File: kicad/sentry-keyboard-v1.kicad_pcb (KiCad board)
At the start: 2 copper layers, 315 x 121 mm, 269 parts, among them J2 Conn_01x04, J4 AVR-ISP-6, SW1 Reset, SW2 RotaryEncoder_Switch, U1 ATmega32U4-AU, Y1 16Mhz

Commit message: Get all components roughly placed
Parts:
- moved D109 109.0 mm to (247.7, 156.2)
- moved D110 97.3 mm to (228.5, 156.4)
- moved D133 96.3 mm to (355.8, 158.2)
- moved D108 88.7 mm to (266.7, 156.2)
- moved D118 83.5 mm to (68.8, 156.2)
- moved D123 80.8 mm to (147.6, 137.2)
- moved D125 76.2 mm to (185.6, 137.1)
- moved D124 76.2 mm to (166.6, 137.2)
- moved D132 76.2 mm to (316.7, 156.2)
- moved D112 76.1 mm to (190.6, 156.2)
- moved D113 76.1 mm to (171.5, 156.2)
- moved D114 76.1 mm to (152.4, 156.2)
- moved D115 76.1 mm to (133.5, 156.2)
- moved D116 76.1 mm to (114.5, 156.2)
- moved D127 76.0 mm to (223.6, 137.0)
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
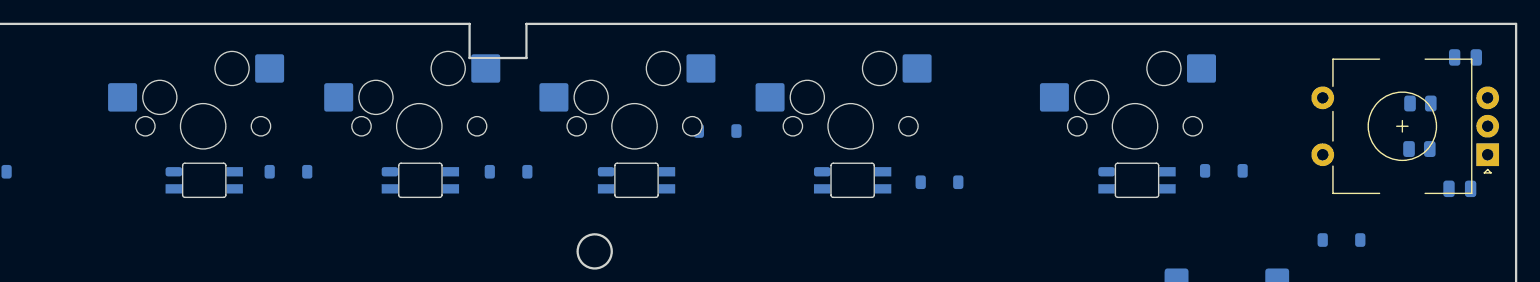
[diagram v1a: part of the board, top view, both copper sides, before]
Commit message: Get the last footprints roughed in.
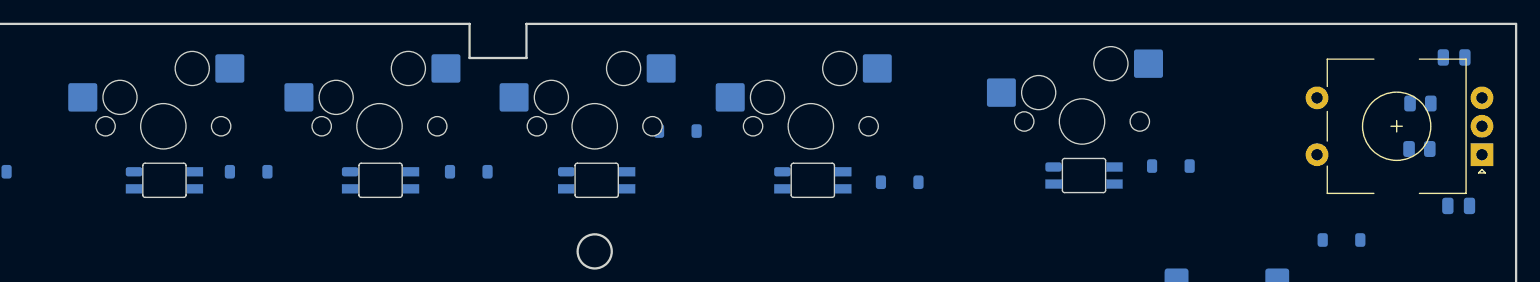
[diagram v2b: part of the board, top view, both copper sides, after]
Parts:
- moved D164 4.68 mm to (328.5, 94.8)
- moved D35 4.68 mm to (336.1, 94.0)
- moved F13 4.68 mm to (328.3, 90.1)
- moved D160 3.50 mm to (247.7, 95.2)
- moved D161 3.50 mm to (266.7, 95.2)
- moved D162 3.50 mm to (285.7, 95.2)
- moved D163 3.50 mm to (304.7, 95.2)
- moved D32 3.50 mm to (274.4, 94.5)
- moved D33 3.50 mm to (292.8, 90.9)
- moved D34 3.50 mm to (312.3, 95.4)
- moved F10 3.50 mm to (266.6, 90.5)
- moved F11 3.50 mm to (285.5, 90.5)
- moved F12 3.50 mm to (304.5, 90.5)
- moved F9 3.50 mm to (247.6, 90.5)
- moved D31 3.50 mm to (255.1, 94.5)
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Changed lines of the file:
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@@
 	(footprint "Keebio:RotaryEncoder_EC11"
 		(layer "F.Cu")
-		(at 356.5 90.5 180)
+		(at 356 90.5 180)
 		(descr "Alps rotary encoder, EC12E... with switch, vertical shaft, http://www.alps.com/prod/info/E/HTML/Encoder/Incremental/EC11/EC11E15204A3.html")
 		(tags "rotary encoder")
@@
 	(footprint "Keebio:SK6812-MINI-E"
 		(layer "B.Cu")
-		(at 251.175 95.25 180)
+		(at 247.675 95.25 180)
 		(property "Reference" "D160"
 			(at 0 -2.1 0)
@@
 	(footprint "Diode_SMD:D_SOD-123"
 		(layer "B.Cu")
-		(at 277.93 94.5 180)
+		(at 274.43 94.5 180)
 		(descr "SOD-123")
 		(tags "SOD-123")
@@
 	(footprint "Keebio:SK6812-MINI-E"
 		(layer "B.Cu")
-		(at 289.175 95.25 180)
+		(at 285.675 95.25 180)
 		(property "Reference" "D162"
 			(at 0 -2.1 0)
@@
 	(footprint "Diode_SMD:D_SOD-123"
 		(layer "B.Cu")
-		(at 315.81 95.42 180)
+		(at 312.31 95.42 180)
 		(descr "SOD-123")
 		(tags "SOD-123")
@@
 	(footprint "Diode_SMD:D_SOD-123"
 		(layer "B.Cu")
-		(at 258.58 94.5 180)
+		(at 255.08 94.5 180)
 		(descr "SOD-123")
 		(tags "SOD-123")
@@
 	(footprint "Kaihl hotswap:MX-Hotswap-1U"
 		(layer "B.Cu")
-		(at 251.08 90.5 180)
+		(at 247.58 90.5 180)
 		(property "Reference" "F9"
 			(at 0 -3.175 0)
@@
 	(footprint "Diode_SMD:D_SOD-123"
 		(layer "B.Cu")
-		(at 340.81 94.42 180)
+		(at 336.15 94 180)
 		(descr "SOD-123")
 		(tags "SOD-123")
@@
 	(footprint "Kaihl hotswap:MX-Hotswap-1U"
 		(layer "B.Cu")
-		(at 270.08 90.5 180)
+		(at 266.58 90.5 180)
 		(property "Reference" "F10"
 			(at 0 -3.175 0)
@@
 	(footprint "Diode_SMD:D_SOD-123"
 		(layer "B.Cu")
-		(at 296.31 90.92 180)
+		(at 292.81 90.92 180)
 		(descr "SOD-123")
 		(tags "SOD-123")
@@
 	(footprint "Kaihl hotswap:MX-Hotswap-1U"
 		(layer "B.Cu")
-		(at 308 90.5 180)
+		(at 304.5 90.5 180)
 		(property "Reference" "F12"
 			(at 0 -3.175 0)
@@
 	(footprint "Keebio:SK6812-MINI-E"
 		(layer "B.Cu")
-		(at 270.175 95.25 180)
+		(at 266.675 95.25 180)
 		(property "Reference" "D161"
 			(at 0 -2.1 0)
@@
 	(footprint "Capacitor_SMD:C_0805_2012Metric"
 		(layer "B.Cu")
-		(at 362.05 84.45 180)
+		(at 361.05 84.45 180)
 		(descr "Capacitor SMD 0805 (2012 Metric), square (rectangular) end terminal, IPC-7351 nominal, (Body size source: IPC-SM-782 page 76, https://www.pcb-3d.com/wordpress/wp-content/uploads/ipc-sm-782a_amendment_1_and_2.pdf, https://docs.google.com/spreadsheets/d/1BsfQQcO9C6DZCsRaXUlFlo91Tg2WpOkGARC1WS5S8t0/edit?usp=sharing), generated with kicad-footprint-generator")
 		(tags "capacitor")
@@
 	(footprint "Kaihl hotswap:MX-Hotswap-1U"
 		(layer "B.Cu")
-		(at 289 90.5 180)
+		(at 285.5 90.5 180)
 		(property "Reference" "F11"
 			(at 0 0.825 0)
@@
 	(footprint "Capacitor_SMD:C_0805_2012Metric"
 		(layer "B.Cu")
-		(at 361.55 96 180)
+		(at 361.45 97.5)
 		(descr "Capacitor SMD 0805 (2012 Metric), square (rectangular) end terminal, IPC-7351 nominal, (Body size source: IPC-SM-782 page 76, https://www.pcb-3d.com/wordpress/wp-content/uploads/ipc-sm-782a_amendment_1_and_2.pdf, https://docs.google.com/spreadsheets/d/1BsfQQcO9C6DZCsRaXUlFlo91Tg2WpOkGARC1WS5S8t0/edit?usp=sharing), generated with kicad-footprint-generator")
 		(tags "capacitor")
@@
 		(attr smd)
 		(fp_line
-			(start -0.261252 0.735)
-			(end 0.261252 0.735)
+			(start -0.261252 -0.735)
+			(end 0.261252 -0.735)
 			(stroke
 				(width 0.12)
@@
 		)
 		(fp_line
-			(start -0.261252 -0.735)
-			(end 0.261252 -0.735)
+			(start -0.261252 0.735)
+			(end 0.261252 0.735)
 			(stroke
 				(width 0.12)
@@
 		)
 		(pad "1" smd roundrect
-			(at -0.95 0 180)
+			(at -0.95 0)
 			(size 1 1.45)
 			(layers "B.Cu" "B.Mask" "B.Paste")
@@
 		)
 		(pad "2" smd roundrect
-			(at 0.95 0 180)
+			(at 0.95 0)
 			(size 1 1.45)
 			(layers "B.Cu" "B.Mask" "B.Paste")
@@
 	(footprint "Keebio:SK6812-MINI-E"
 		(layer "B.Cu")
-		(at 333.175 95.25 180)
+		(at 328.515 94.83 180)
 		(property "Reference" "D164"
 			(at 0 -2.1 0)
@@
 	(footprint "Kaihl hotswap:MX-Hotswap-1U"
 		(layer "B.Cu")
-		(at 333 90.5 180)
+		(at 328.34 90.08 180)
 		(property "Reference" "F13"
 			(at 0 -3.175 0)
@@
 	(footprint "Keebio:SK6812-MINI-E"
 		(layer "B.Cu")
-		(at 308.175 95.25 180)
+		(at 304.675 95.25 180)
 		(property "Reference" "D163"
 			(at 0 -2.1 0)
@@
 			(layer "F.Cu")
 			(effects
+				(font
+					(size 1.5 1.5)
+					(thickness 0.3)
+				)
+			)
+		)
+	)
+	(dimension
+		(type orthogonal)
+		(layer "F.Cu")
+		(pts
+			(xy 51.5 83) (xy 334.5 94)
+		)
+		(height -6.5)
+		(orientation 0)
+		(format
+			(prefix "")
+			(suffix "")
+			(units 2)
+			(units_format 0)
+			(precision 4)
+			(suppress_zeroes yes)
+		)
+		(style
+			(thickness 0.2)
+			(arrow_length 1.27)
+			(text_position_mode 0)
+			(arrow_direction outward)
+			(extension_height 0.58642)
+			(extension_offset 0.5)
+			(keep_text_aligned yes)
+		)
+		(gr_text "283"
+			(at 193 74.7 0)
+			(layer "F.Cu")
+			(effects

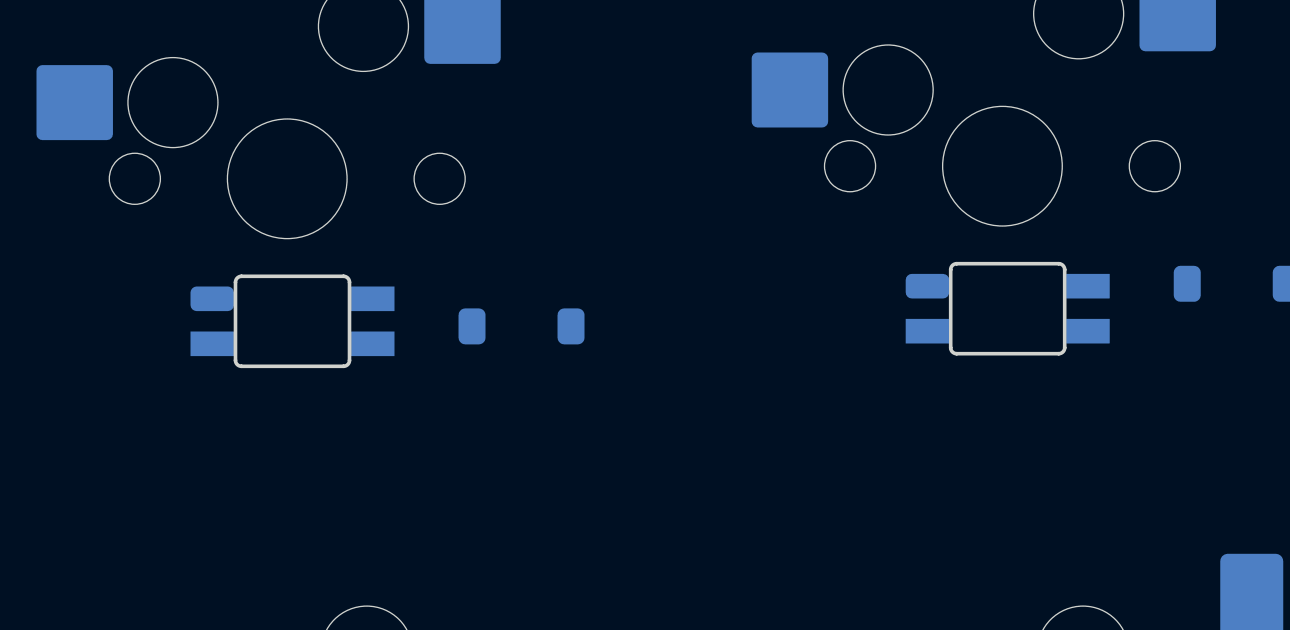
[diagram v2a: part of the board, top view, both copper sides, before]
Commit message: Fix silkscreen
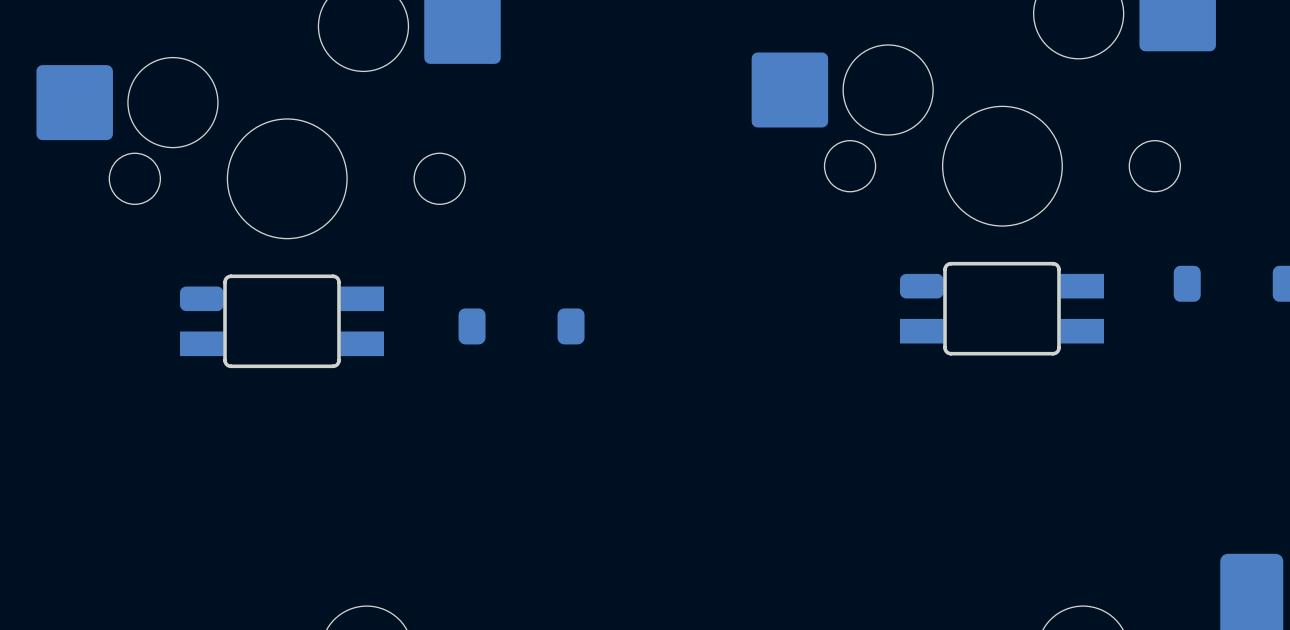
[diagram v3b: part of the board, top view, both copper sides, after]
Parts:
- moved D163 0.35 mm to (304.3, 95.2)
- moved D164 0.19 mm to (328.3, 94.8)
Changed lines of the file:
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@@
 		(at 276.161666 170.409951 180)
 		(property "Reference" "MX/1"
-			(at 0 0.825 0)
+			(at 0 -3.090049 0)
 			(layer "B.Fab")
 			(effects
@@
 		)
 		(property "Value" "K0_4"
-			(at -27.25 4.8334 0)
+			(at 0.161666 7.909951 0)
 			(layer "Dwgs.User")
 			(effects
@@
 	(footprint "Keebio:SK6812-MINI-E"
 		(layer "B.Cu")
-		(at 328.515 94.83 180)
+		(at 328.325 94.83 180)
 		(property "Reference" "D164"
 			(at 0 -2.1 0)
@@
 	(footprint "Keebio:SK6812-MINI-E"
 		(layer "B.Cu")
-		(at 304.675 95.25 180)
+		(at 304.325 95.25 180)
 		(property "Reference" "D163"
 			(at 0 -2.1 0)

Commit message: Fix a bunch of alignment issues.
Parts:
- moved D33 3.54 mm to (293.7, 94.3)
- moved D34 1.01 mm to (312.6, 94.5)
- moved D107 0.65 mm to (285.7, 156.1)
- moved D8 0.59 mm to (88.8, 117.3)
- moved D164 0.42 mm to (328.3, 95.2)
- moved D35 0.42 mm to (336.1, 94.4)
- moved F13 0.42 mm to (328.3, 90.5)
- moved D111 0.37 mm to (209.4, 156.2)
- moved D158 0.36 mm to (204.8, 95.3)
- moved D159 0.36 mm to (223.8, 95.3)
- moved D29 0.36 mm to (212.3, 94.5)
- moved D30 0.36 mm to (231.8, 94.5)
- moved F8 0.36 mm to (223.7, 90.5)
- moved F7 0.36 mm to (204.6, 90.5)
- moved D116 0.34 mm to (114.2, 156.2)
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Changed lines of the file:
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@@
 	(footprint "Keebio:SK6812-MINI-E"
 		(layer "B.Cu")
-		(at 73.568415 175.5 180)
+		(at 73.659838 175.364558 180)
 		(property "Reference" "D87"
 			(at 0 -2.1 0)
@@
 	(footprint "Keebio:SK6812-MINI-E"
 		(layer "B.Cu")
-		(at 85.325 95.25 180)
+		(at 85.511493 95.23019 180)
 		(property "Reference" "D152"
 			(at 0 -2.1 0)
@@
 	(footprint "Keebio:SK6812-MINI-E"
 		(layer "B.Cu")
-		(at 228.481642 156.361149 180)
+		(at 228.481642 156.25 180)
 		(property "Reference" "D110"
 			(at 0 -2.1 0)
@@
 	(footprint "Keebio:SK6812-MINI-E"
 		(layer "B.Cu")
-		(at 355.825 158.25 180)
+		(at 355.838748 158.332964 180)
 		(property "Reference" "D133"
 			(at 0 -2.1 0)
@@
 	(footprint "Keebio:SK6812-MINI-E"
 		(layer "B.Cu")
-		(at 224.175 95.25 180)
+		(at 223.820494 95.268755 180)
 		(property "Reference" "D159"
 			(at 0 -2.1 0)
@@
 	(footprint "Keebio:SK6812-MINI-E"
 		(layer "B.Cu")
-		(at 104.620246 175.234122 180)
+		(at 104.617952 175.285178 180)
 		(property "Reference" "D88"
 			(at 0 -2.1 0)
@@
 	(footprint "Diode_SMD:D_SOD-123"
 		(layer "B.Cu")
-		(at 89.382684 117.299657 180)
+		(at 88.798308 117.251157 180)
 		(descr "SOD-123")
 		(tags "SOD-123")
@@
 	(footprint "Keebio:SK6812-MINI-E"
 		(layer "B.Cu")
-		(at 285.675 95.25 180)
+		(at 285.831254 95.252822 180)
 		(property "Reference" "D162"
 			(at 0 -2.1 0)
@@
 	(footprint "Diode_SMD:D_SOD-123"
 		(layer "B.Cu")
-		(at 312.31 95.42 180)
+		(at 312.620548 94.46296 180)
 		(descr "SOD-123")
 		(tags "SOD-123")
@@
 	(footprint "Keebio:SK6812-MINI-E"
 		(layer "B.Cu")
-		(at 104.325 95.25 180)
+		(at 104.612253 95.202627 180)
 		(property "Reference" "D153"
 			(at 0 -2.1 0)
@@
 	(footprint "Diode_SMD:D_SOD-123"
 		(layer "B.Cu")
-		(at 255.08 94.5 180)
+		(at 255.400906 94.424033 180)
 		(descr "SOD-123")
 		(tags "SOD-123")
@@
 	(footprint "Diode_SMD:D_SOD-123"
 		(layer "B.Cu")
-		(at 232.15 94.5 180)
+		(at 231.795494 94.518755 180)
 		(descr "SOD-123")
 		(tags "SOD-123")
@@
 	(footprint "Diode_SMD:D_SOD-123"
 		(layer "B.Cu")
-		(at 336.15 94 180)
+		(at 336.15 94.42 180)
 		(descr "SOD-123")
 		(tags "SOD-123")
@@
 	(footprint "Keebio:SK6812-MINI-E"
 		(layer "B.Cu")
-		(at 285.675 156.75 180)
+		(at 285.69876 156.10455 180)
 		(property "Reference" "D107"
 			(at 0 -2.1 0)
@@
 	(footprint "Keebio:SK6812-MINI-E"
 		(layer "B.Cu")
-		(at 355.675 177.75 180)
+		(at 355.640299 177.455276 180)
 		(property "Reference" "D103"
 			(at 0 -2.1 0)
@@
 	(footprint "Keebio:SK6812-MINI-E"
 		(layer "B.Cu")
-		(at 152.427098 156.23958 180)
+		(at 152.231333 156.216925 180)
 		(property "Reference" "D114"
 			(at 0 -2.1 0)
@@
 	(footprint "Keebio:SK6812-MINI-E"
 		(layer "B.Cu")
-		(at 114.530698 156.227879 180)
+		(at 114.195188 156.150775 180)
 		(property "Reference" "D116"
 			(at 0 -2.1 0)
@@
 	(footprint "Kaihl hotswap:MX-Hotswap-1U"
 		(layer "B.Cu")
-		(at 205 90.5 180)
+		(at 204.645494 90.518755 180)
 		(property "Reference" "F7"
 			(at 0 -3.175 0)
@@
 	(footprint "Keebio:SK6812-MINI-E"
 		(layer "B.Cu")
-		(at 133.474849 156.23958 180)
+		(at 133.38677 156.216925 180)
 		(property "Reference" "D115"
 			(at 0 -2.1 0)
@@
 	(footprint "Keebio:SK6812-MINI-E"
 		(layer "B.Cu")
-		(at 209.717024 156.45991 180)
+		(at 209.446173 156.213048 180)
 		(property "Reference" "D111"
 			(at 0 -2.1 0)
@@
 	(footprint "Keebio:SK6812-MINI-E"
 		(layer "B.Cu")
-		(at 205.175 95.25 180)
+		(at 204.820494 95.268755 180)
 		(property "Reference" "D158"
 			(at 0 -2.1 0)
@@
 	(footprint "Diode_SMD:D_SOD-123"
 		(layer "B.Cu")
-		(at 292.81 90.92 180)
+		(at 293.701842 94.348117 180)
 		(descr "SOD-123")
 		(tags "SOD-123")
@@
 	(footprint "Keebio:SK6812-MINI-E"
 		(layer "B.Cu")
-		(at 95.325 156.25 180)
+		(at 95.052688 156.154651 180)
 		(property "Reference" "D117"
 			(at 0 -2.1 0)
@@
 	(footprint "Kaihl hotswap:MX-Hotswap-1U"
 		(layer "B.Cu")
-		(at 304.5 90.5 180)
+		(at 304.656254 90.502822 180)
 		(property "Reference" "F12"
 			(at 0 -3.175 0)
@@
 	(footprint "Keebio:SK6812-MINI-E"
 		(layer "B.Cu")
-		(at 190.550241 156.195897 180)
+		(at 190.50875 156.122251 180)
 		(property "Reference" "D112"
 			(at 0 -2.1 0)
@@
 	(footprint "Diode_SMD:D_SOD-123"
 		(layer "B.Cu")
-		(at 131.43 94 180)
+		(at 131.4295 94.314815 180)
 		(descr "SOD-123")
 		(tags "SOD-123")
@@
 	(footprint "Kaihl hotswap:MX-Hotswap-1U"
 		(layer "B.Cu")
-		(at 224.08 90.5 180)
+		(at 223.725494 90.518755 180)
 		(property "Reference" "F8"
 			(at 0 -3.175 0)
@@
 	(footprint "Kaihl hotswap:MX-Hotswap-1U"
 		(layer "B.Cu")
-		(at 285.5 90.5 180)
+		(at 285.656254 90.502822 180)
 		(property "Reference" "F11"
 			(at 0 0.825 0)
@@
 	(footprint "Keebio:SK6812-MINI-E"
 		(layer "B.Cu")
-		(at 328.325 94.83 180)
+		(at 328.325 95.25 180)
 		(property "Reference" "D164"
 			(at 0 -2.1 0)
@@
 	(footprint "Kaihl hotswap:MX-Hotswap-1U"
 		(layer "B.Cu")
-		(at 328.34 90.08 180)
+		(at 328.34 90.5 180)
 		(property "Reference" "F13"
 			(at 0 -3.175 0)
@@
 	(footprint "Diode_SMD:D_SOD-123"
 		(layer "B.Cu")
-		(at 212.65 94.5 180)
+		(at 212.295494 94.518755 180)
 		(descr "SOD-123")
 		(tags "SOD-123")
@@
 	(footprint "Keebio:SK6812-MINI-E"
 		(layer "B.Cu")
-		(at 304.325 95.25 180)
+		(at 304.481254 95.252822 180)
 		(property "Reference" "D163"
 			(at 0 -2.1 0)
